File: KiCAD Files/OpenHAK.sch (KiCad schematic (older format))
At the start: 41 parts, among them P1 CONN_01X10, P2 USB_OTG, Q1 Q_NMOS_GSD, Q2 Q_NMOS_GSD, U1 rfd_77101, U2 MAX30100, U3 NCP551, U4 BMI160, U5 MCP73831, U6 NCP551

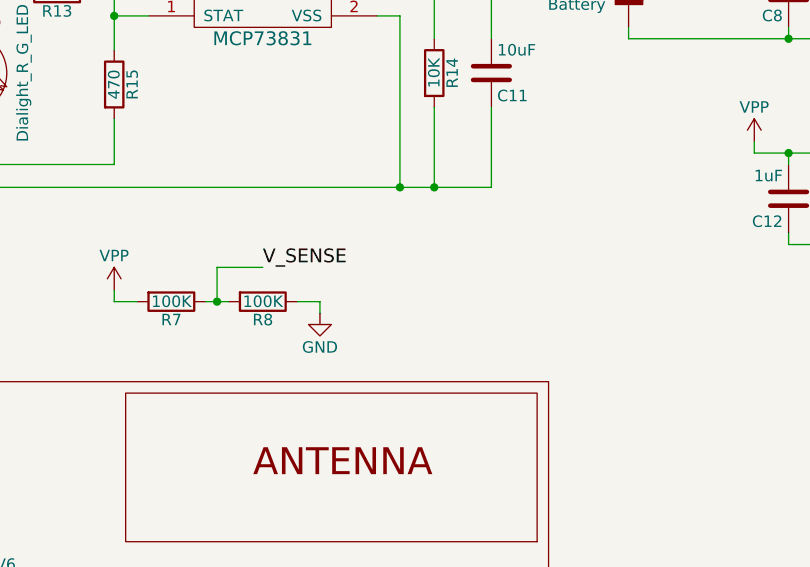
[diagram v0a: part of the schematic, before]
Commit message: Added cap to VSENS to fix battery reading
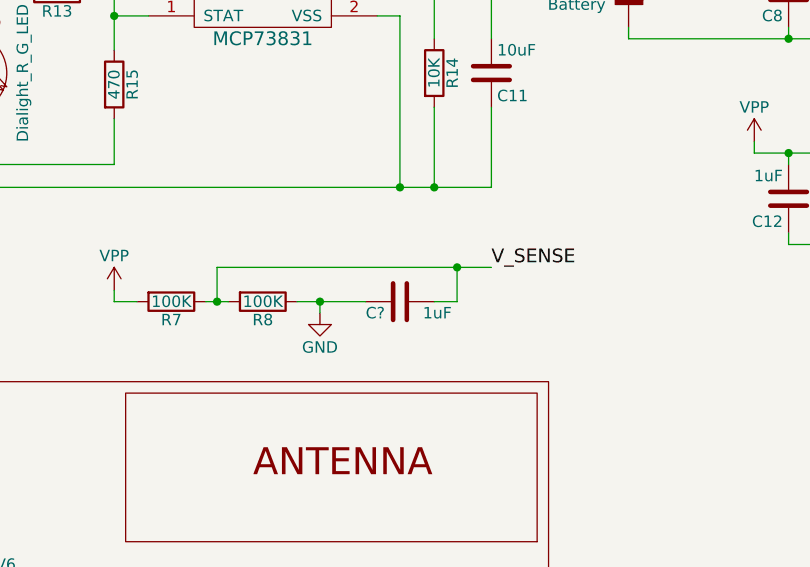
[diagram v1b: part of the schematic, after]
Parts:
- added C?: 1uF, Capacitors_SMD:C_0603, symbol C
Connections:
- net GND: now also C?.2
- net V_SENSE: now also C?.1
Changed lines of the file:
@@
 LIBS:contrib
 LIBS:valves
-LIBS:OpenHAK_beta-cache
+LIBS:OpenHAK-cache
 EELAYER 25 0
 EELAYER END
@@
 	0    1    1    0
 $EndComp
-Text Label 3450 2550 0    60   ~ 0
+Text Label 4450 2550 0    60   ~ 0
 V_SENSE
 $Comp
@@
 	3200 2700 3300 2700
 Wire Wire Line
-	3600 2700 3700 2700
+	3600 2700 3900 2700
 Wire Wire Line
 	3700 2700 3700 2750
@@
 	3250 2700 3250 2550
 Wire Wire Line
-	3250 2550 3450 2550
+	3250 2550 4450 2550
 Connection ~ 3250 2700
 Wire Wire Line
@@
 Text Label 2950 6500 3    60   ~ 0
 V_SENSE
+$Comp
+L C C?
+U 1 1 5A972CCB
+P 4050 2700
+F 0 "C?" V 4100 2550 50  0000 L CNN
+F 1 "1uF" V 4100 2800 50  0000 L CNN
+F 2 "Capacitors_SMD:C_0603" H 4088 2550 50  0001 C CNN
+F 3 "" H 4050 2700 50  0000 C CNN
+	1    4050 2700
+	0    1    1    0
+$EndComp
+Connection ~ 3700 2700
+Wire Wire Line
+	4200 2700 4300 2700
+Wire Wire Line
+	4300 2700 4300 2550
+Connection ~ 4300 2550
 $EndSCHEMATC
